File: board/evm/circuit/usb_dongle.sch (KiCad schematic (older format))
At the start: 1 part

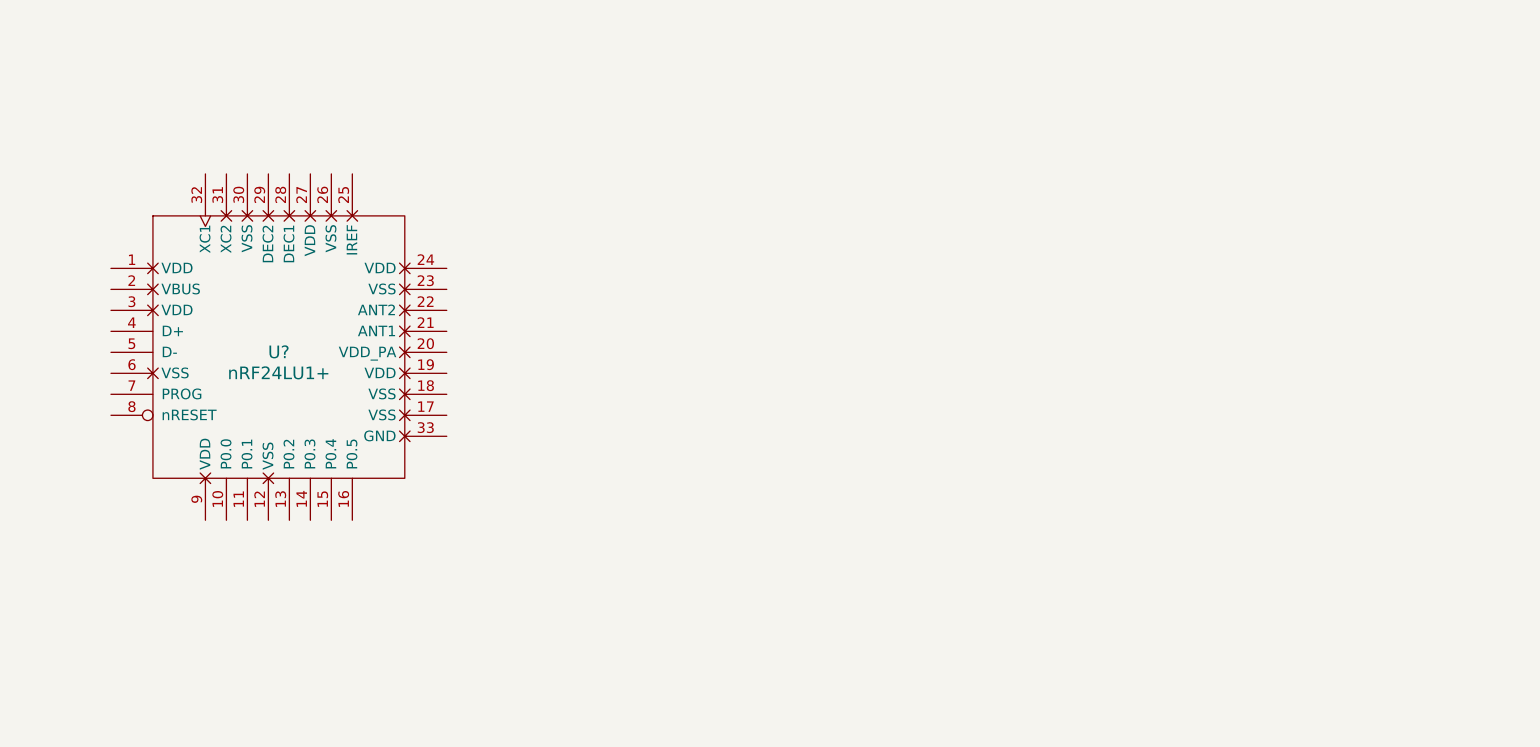
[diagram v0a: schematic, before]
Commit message: still working for sch
All done except for battery, which need more consideration on scheme of
QC2.0 (or QC3.0?), bidirectional charge.
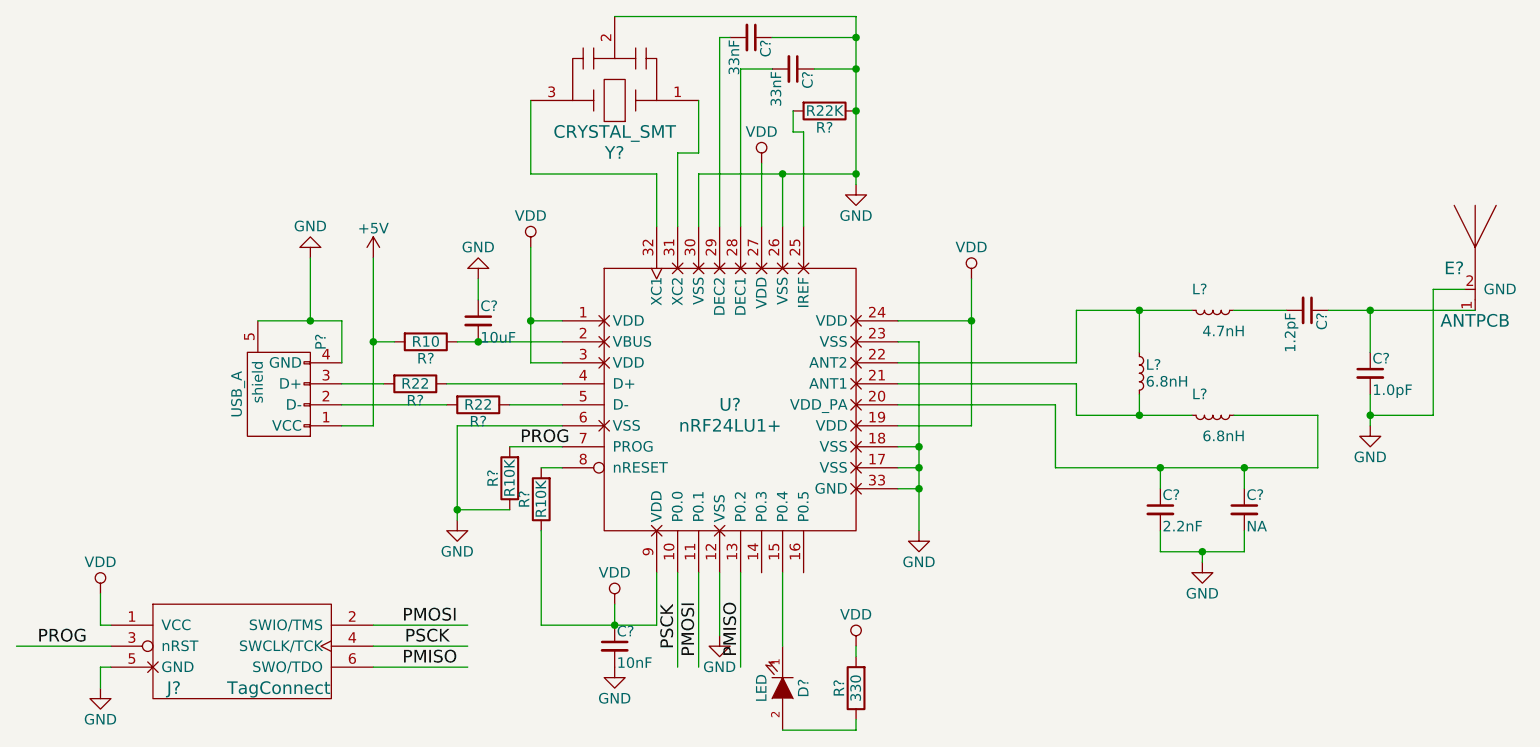
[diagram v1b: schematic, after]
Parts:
- added C?: 10uF, symbol C_Small
- added C?: 10nF, symbol C_Small
- added C? (x2): 33nF, symbol C_Small
- added C?: 2.2nF, symbol C_Small
- added C?: NA, symbol C_Small
- added C?: 1.2pF, symbol C_Small
- added C?: 1.0pF, symbol C_Small
- added D?: LED, symbol LED
- added E?: ANTPCB, symbol ANTPCB
- added J?: TagConnect, symbol TagConnect
- added L? (x2): 6.8nH, symbol L_Small
- added L?: 4.7nH, symbol L_Small
- added P?: USB_A, symbol USB_A
- added R? (x2): R22, symbol R
- added R?: R10, symbol R
- added R? (x2): R10K, symbol R
- added R?: R22K, symbol R
- added R?: 330, symbol R
- added Y?: CRYSTAL_SMT, symbol CRYSTAL_SMT
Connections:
- net labels added: +5V, GND, PMISO, PMOSI, PROG, PSCK, VDD
- wire segments 0 -> 117
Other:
- moved on the sheet: U?

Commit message: bug fix
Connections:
- wire segments 117 -> 95
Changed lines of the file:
@@
 LIBS:Altera
 LIBS:my_kicad
+LIBS:Oscillators
 LIBS:oh-my-keyboard-cache
 EELAYER 25 0
@@
 $Descr A3 16535 11693
 encoding utf-8
-Sheet 7 12
+Sheet 6 12
 Title ""
 Date ""
@@
 	4600 3100 4850 3100
 Wire Wire Line
-	3400 2700 3650 2700
-Wire Wire Line
-	3650 2700 3800 2700
+	3400 2700 3800 2700
 Wire Wire Line
 	3800 2700 3800 2900
@@
 	4850 2700 4700 2700
 Wire Wire Line
-	4700 2350 4700 2700
-Wire Wire Line
-	4700 2700 4700 2900
+	4700 2350 4700 2900
 Wire Wire Line
 	4700 2900 4850 2900
@@
 	4050 2800 3950 2800
 Wire Wire Line
-	4350 2800 4450 2800
-Wire Wire Line
-	4450 2800 4850 2800
+	4350 2800 4850 2800
 Connection ~ 4450 2800
 Wire Wire Line
-	3950 2400 3950 2800
-Wire Wire Line
-	3950 2800 3950 3200
+	3950 2400 3950 3200
 Wire Wire Line
 	4450 2600 4450 2500
@@
 	4850 3200 4350 3200
 Wire Wire Line
-	4350 3200 4350 3600
-Wire Wire Line
-	4350 3600 4350 3650
+	4350 3200 4350 3650
 Wire Wire Line
 	4600 3600 4350 3600
@@
 	4750 3700 4750 4150
 Wire Wire Line
-	4750 4150 5100 4150
-Wire Wire Line
-	5100 4150 5300 4150
+	4750 4150 5300 4150
 Wire Wire Line
 	5100 4150 5100 4050
@@
 	6450 3300 6550 3300
 Wire Wire Line
-	6550 2800 6550 3300
-Wire Wire Line
-	6550 3300 6550 3400
-Wire Wire Line
-	6550 3400 6550 3500
-Wire Wire Line
-	6550 3500 6550 3700
+	6550 2800 6550 3700
 Wire Wire Line
 	6450 3500 6550 3500
@@
 	6450 2700 6800 2700
 Wire Wire Line
-	6800 2500 6800 2700
-Wire Wire Line
-	6800 2700 6800 3200
+	6800 2500 6800 3200
 Wire Wire Line
 	6800 3200 6450 3200
@@
 	5500 2000 5500 2250
 Wire Wire Line
-	6250 2000 5900 2000
-Wire Wire Line
-	5900 2000 5500 2000
-Wire Wire Line
-	6250 1250 6250 1350
-Wire Wire Line
-	6250 1350 6250 1500
-Wire Wire Line
-	6250 1500 6250 1700
-Wire Wire Line
-	6250 1700 6250 2000
-Wire Wire Line
-	6250 2000 6250 2050
+	6250 2000 5500 2000
+Wire Wire Line
+	6250 1250 6250 2050
 Wire Wire Line
 	5900 2250 5900 2000
@@
 $EndComp
 Wire Wire Line
-	7300 2650 7600 2650
-Wire Wire Line
-	7600 2650 7850 2650
+	7300 2650 7850 2650
 Wire Wire Line
 	7600 2650 7600 2850
@@
 	7600 3050 7600 3150
 Wire Wire Line
-	7300 3150 7600 3150
-Wire Wire Line
-	7600 3150 7850 3150
+	7300 3150 7850 3150
 Wire Wire Line
 	6450 2900 7300 2900
@@
 	7200 3100 7200 3400
 Wire Wire Line
-	7200 3400 7700 3400
-Wire Wire Line
-	7700 3400 8100 3400
-Wire Wire Line
-	8100 3400 8450 3400
+	7200 3400 8450 3400
 Wire Wire Line
 	8450 3400 8450 3150
@@
 	7700 3700 7700 3800
 Wire Wire Line
-	7700 3800 7900 3800
-Wire Wire Line
-	7900 3800 8100 3800
+	7700 3800 8100 3800
 Wire Wire Line
 	8100 3800 8100 3700
@@
 $EndComp
 Wire Wire Line
-	8500 2650 8700 2650
-Wire Wire Line
-	8700 2650 9200 2650
+	8500 2650 9200 2650
 Wire Wire Line
 	8700 2650 8700 2850
@@
 $EndComp
 Wire Wire Line
-	8700 3050 8700 3150
-Wire Wire Line
-	8700 3150 8700 3200
+	8700 3050 8700 3200
 $Comp
 L ANTPCB E?

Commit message: working on drc
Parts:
- gave numbers to parts that had none: 24
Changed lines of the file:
@@
 $EndDescr
 $Comp
-L nRF24LU1+ U?
+L nRF24LU1+ U9
 U 1 1 5754763F
 P 5650 3100
-F 0 "U?" H 5650 3100 60  0000 C CNN
+F 0 "U9" H 5650 3100 60  0000 C CNN
 F 1 "nRF24LU1+" H 5650 3000 60  0000 C CNN
 F 2 "" H 5650 3100 60  0000 C CNN
@@
 $EndComp
 $Comp
-L USB_A P?
+L USB_A P2
 U 1 1 5758AC51
 P 3500 3000
-F 0 "P?" H 3700 2800 50  0000 C CNN
+F 0 "P2" H 3700 2800 50  0000 C CNN
 F 1 "USB_A" H 3450 3200 50  0000 C CNN
 F 2 "" V 3450 2900 50  0000 C CNN
@@
 $EndComp
 $Comp
-L R R?
+L R R8
 U 1 1 5758AF6E
 P 4150 3000
-F 0 "R?" V 4230 3000 50  0000 C CNN
+F 0 "R8" V 4230 3000 50  0000 C CNN
 F 1 "R22" V 4150 3000 50  0000 C CNN
 F 2 "" V 4080 3000 50  0000 C CNN
@@
 $EndComp
 $Comp
-L R R?
+L R R10
 U 1 1 5758AFBE
 P 4450 3100
-F 0 "R?" V 4530 3100 50  0000 C CNN
+F 0 "R10" V 4530 3100 50  0000 C CNN
 F 1 "R22" V 4450 3100 50  0000 C CNN
 F 2 "" V 4380 3100 50  0000 C CNN
@@
 $EndComp
 $Comp
-L GND #PWR?
+L GND #PWR080
 U 1 1 5758B050
 P 3650 2400
-F 0 "#PWR?" H 3650 2150 50  0001 C CNN
+F 0 "#PWR080" H 3650 2150 50  0001 C CNN
 F 1 "GND" H 3650 2250 50  0000 C CNN
 F 2 "" H 3650 2400 50  0000 C CNN
@@
 $EndComp
 $Comp
-L +5V #PWR?
+L +5V #PWR081
 U 1 1 5758B200
 P 3950 2400
-F 0 "#PWR?" H 3950 2250 50  0001 C CNN
+F 0 "#PWR081" H 3950 2250 50  0001 C CNN
 F 1 "+5V" H 3950 2540 50  0000 C CNN
 F 2 "" H 3950 2400 50  0000 C CNN
@@
 $EndComp
 $Comp
-L C_Small C?
+L C_Small C28
 U 1 1 5758B23D
 P 4450 2700
-F 0 "C?" H 4460 2770 50  0000 L CNN
+F 0 "C28" H 4460 2770 50  0000 L CNN
 F 1 "10uF" H 4460 2620 50  0000 L CNN
 F 2 "" H 4450 2700 50  0000 C CNN
@@
 $EndComp
 $Comp
-L R R?
+L R R9
 U 1 1 5758B396
 P 4200 2800
-F 0 "R?" V 4280 2800 50  0000 C CNN
+F 0 "R9" V 4280 2800 50  0000 C CNN
 F 1 "R10" V 4200 2800 50  0000 C CNN
 F 2 "" V 4130 2800 50  0000 C CNN
@@
 $EndComp
 $Comp
-L GND #PWR?
+L GND #PWR082
 U 1 1 5758B547
 P 4450 2500
-F 0 "#PWR?" H 4450 2250 50  0001 C CNN
+F 0 "#PWR082" H 4450 2250 50  0001 C CNN
 F 1 "GND" H 4450 2350 50  0000 C CNN
 F 2 "" H 4450 2500 50  0000 C CNN
@@
 $EndComp
 $Comp
-L GND #PWR?
+L GND #PWR083
 U 1 1 5758B5D1
 P 4350 3650
-F 0 "#PWR?" H 4350 3400 50  0001 C CNN
+F 0 "#PWR083" H 4350 3400 50  0001 C CNN
 F 1 "GND" H 4350 3500 50  0000 C CNN
 F 2 "" H 4350 3650 50  0000 C CNN
@@
 $EndComp
 $Comp
-L R R?
+L R R11
 U 1 1 5758B6D5
 P 4600 3450
-F 0 "R?" V 4680 3450 50  0000 C CNN
+F 0 "R11" V 4680 3450 50  0000 C CNN
 F 1 "R10K" V 4600 3450 50  0000 C CNN
 F 2 "" V 4530 3450 50  0000 C CNN
@@
 $EndComp
 $Comp
-L R R?
+L R R12
 U 1 1 5758B784
 P 4750 3550
-F 0 "R?" V 4830 3550 50  0000 C CNN
+F 0 "R12" V 4830 3550 50  0000 C CNN
 F 1 "R10K" V 4750 3550 50  0000 C CNN
 F 2 "" V 4680 3550 50  0000 C CNN
@@
 $EndComp
 $Comp
-L C_Small C?
+L C_Small C29
 U 1 1 5758BA18
 P 5100 4250
-F 0 "C?" H 5110 4320 50  0000 L CNN
+F 0 "C29" H 5110 4320 50  0000 L CNN
 F 1 "10nF" H 5110 4170 50  0000 L CNN
 F 2 "" H 5100 4250 50  0000 C CNN
@@
 $EndComp
 $Comp
-L GND #PWR?
+L GND #PWR084
 U 1 1 5758BAA4
 P 5100 4350
-F 0 "#PWR?" H 5100 4100 50  0001 C CNN
+F 0 "#PWR084" H 5100 4100 50  0001 C CNN
 F 1 "GND" H 5100 4200 50  0000 C CNN
 F 2 "" H 5100 4350 50  0000 C CNN
@@
 $EndComp
 $Comp
-L GND #PWR?
+L GND #PWR085
 U 1 1 5758BAF2
 P 5600 4200
-F 0 "#PWR?" H 5600 3950 50  0001 C CNN
+F 0 "#PWR085" H 5600 3950 50  0001 C CNN
 F 1 "GND" H 5600 4050 50  0000 C CNN
 F 2 "" H 5600 4200 50  0000 C CNN
@@
 $EndComp
 $Comp
-L GND #PWR?
+L GND #PWR086
 U 1 1 5758BCC4
 P 6550 3700
-F 0 "#PWR?" H 6550 3450 50  0001 C CNN
+F 0 "#PWR086" H 6550 3450 50  0001 C CNN
 F 1 "GND" H 6550 3550 50  0000 C CNN
 F 2 "" H 6550 3700 50  0000 C CNN
@@
 $EndComp
 $Comp
-L GND #PWR?
+L GND #PWR087
 U 1 1 5758BFC5
 P 6250 2050
-F 0 "#PWR?" H 6250 1800 50  0001 C CNN
+F 0 "#PWR087" H 6250 1800 50  0001 C CNN
 F 1 "GND" H 6250 1900 50  0000 C CNN
 F 2 "" H 6250 2050 50  0000 C CNN
@@
 Connection ~ 5900 2000
 $Comp
-L CRYSTAL_SMT Y?
+L CRYSTAL_SMT Y3
 U 1 1 5758C1C1
 P 5100 1600
-F 0 "Y?" H 5100 1900 60  0000 C CNN
+F 0 "Y3" H 5100 1900 60  0000 C CNN
 F 1 "CRYSTAL_SMT" H 5100 1800 60  0000 C CNN
 F 2 "" H 5100 1600 60  0000 C CNN
@@
 Connection ~ 6250 2000
 $Comp
-L C_Small C?
+L C_Small C30
 U 1 1 5758C579
 P 5750 1350
-F 0 "C?" H 5760 1420 50  0000 L CNN
+F 0 "C30" H 5760 1420 50  0000 L CNN
 F 1 "33nF" H 5760 1270 50  0000 L CNN
 F 2 "" H 5750 1350 50  0000 C CNN
@@
 	5600 1350 5650 1350
 $Comp
-L C_Small C?
+L C_Small C31
 U 1 1 5758C690
 P 5950 1500
-F 0 "C?" H 5960 1570 50  0000 L CNN
+F 0 "C31" H 5960 1570 50  0000 L CNN
 F 1 "33nF" H 5960 1420 50  0000 L CNN
 F 2 "" H 5950 1500 50  0000 C CNN
@@
 Connection ~ 6250 1500
 $Comp
-L R R?
+L R R13
 U 1 1 5758C7CB
 P 6100 1700
-F 0 "R?" V 6180 1700 50  0000 C CNN
+F 0 "R13" V 6180 1700 50  0000 C CNN
 F 1 "R22K" V 6100 1700 50  0000 C CNN
 F 2 "" V 6030 1700 50  0000 C CNN
@@
 Connection ~ 6250 1700
 $Comp
-L L_Small L?
+L L_Small L7
 U 1 1 5758CBB0
 P 7600 2950
-F 0 "L?" H 7630 2990 50  0000 L CNN
+F 0 "L7" H 7630 2990 50  0000 L CNN
 F 1 "6.8nH" H 7630 2910 50  0000 L CNN
 F 2 "" H 7600 2950 50  0000 C CNN
@@
 $EndComp
 $Comp
-L L_Small L?
+L L_Small L8
 U 1 1 5758CC1D
 P 7950 2650
-F 0 "L?" V 7850 2550 50  0000 L CNN
+F 0 "L8" V 7850 2550 50  0000 L CNN
 F 1 "4.7nH" V 8050 2600 50  0000 L CNN
 F 2 "" H 7950 2650 50  0000 C CNN
@@
 $EndComp
 $Comp
-L L_Small L?
+L L_Small L9
 U 1 1 5758CD4B
 P 7950 3150
-F 0 "L?" V 7850 3050 50  0000 L CNN
+F 0 "L9" V 7850 3050 50  0000 L CNN
 F 1 "6.8nH" V 8050 3100 50  0000 L CNN
 F 2 "" H 7950 3150 50  0000 C CNN
@@
 	8450 3150 8050 3150
 $Comp
-L C_Small C?
+L C_Small C32
 U 1 1 5758CFF2
 P 7700 3600
-F 0 "C?" H 7710 3670 50  0000 L CNN
+F 0 "C32" H 7710 3670 50  0000 L CNN
 F 1 "2.2nF" H 7710 3520 50  0000 L CNN
 F 2 "" H 7700 3600 50  0000 C CNN
@@
 $EndComp
 $Comp
-L C_Small C?
+L C_Small C33
 U 1 1 5758D097
 P 8100 3600
-F 0 "C?" H 8110 3670 50  0000 L CNN
+F 0 "C33" H 8110 3670 50  0000 L CNN
 F 1 "NA" H 8110 3520 50  0000 L CNN
 F 2 "" H 8100 3600 50  0000 C CNN
@@
 	8100 3800 8100 3700
 $Comp
-L GND #PWR?
+L GND #PWR088
 U 1 1 5758D27C
 P 7900 3850
-F 0 "#PWR?" H 7900 3600 50  0001 C CNN
+F 0 "#PWR088" H 7900 3600 50  0001 C CNN
 F 1 "GND" H 7900 3700 50  0000 C CNN
 F 2 "" H 7900 3850 50  0000 C CNN
@@
 Connection ~ 7900 3800
 $Comp
-L C_Small C?
+L C_Small C34
 U 1 1 5758D32D
 P 8400 2650
-F 0 "C?" H 8410 2720 50  0000 L CNN
+F 0 "C34" H 8410 2720 50  0000 L CNN
 F 1 "1.2pF" H 8410 2570 50  0000 L CNN
 F 2 "" H 8400 2650 50  0000 C CNN
@@
 	8300 2650 8050 2650
 $Comp
-L C_Small C?
+L C_Small C35
 U 1 1 5758D43B
 P 8700 2950
-F 0 "C?" H 8710 3020 50  0000 L CNN
+F 0 "C35" H 8710 3020 50  0000 L CNN
 F 1 "1.0pF" H 8710 2870 50  0000 L CNN
 F 2 "" H 8700 2950 50  0000 C CNN
@@
 	8700 2650 8700 2850
 $Comp
-L GND #PWR?
+L GND #PWR089
 U 1 1 5758D552
 P 8700 3200
-F 0 "#PWR?" H 8700 2950 50  0001 C CNN
+F 0 "#PWR089" H 8700 2950 50  0001 C CNN
 F 1 "GND" H 8700 3050 50  0000 C CNN
 F 2 "" H 8700 3200 50  0000 C CNN
@@
 	8700 3050 8700 3200
 $Comp
-L ANTPCB E?
+L ANTPCB E3
 U 1 1 5758D612
 P 9200 2600
-F 0 "E?" H 9100 2750 60  0000 C CNN
+F 0 "E3" H 9100 2750 60  0000 C CNN
 F 1 "ANTPCB" H 9200 2500 60  0000 C CNN
 F 2 "" H 9200 2600 60  0000 C CNN
@@
 Connection ~ 8700 3150
 $Comp
-L VDD #PWR?
+L VDD #PWR090
 U 1 1 5758DAF7
 P 4700 2350
-F 0 "#PWR?" H 4700 2200 50  0001 C CNN
+F 0 "#PWR090" H 4700 2200 50  0001 C CNN
 F 1 "VDD" H 4700 2500 50  0000 C CNN
 F 2 "" H 4700 2350 50  0000 C CNN
@@
 $EndComp
 $Comp
-L VDD #PWR?
+L VDD #PWR091
 U 1 1 5758DB5E
 P 5100 4050
-F 0 "#PWR?" H 5100 3900 50  0001 C CNN
+F 0 "#PWR091" H 5100 3900 50  0001 C CNN
 F 1 "VDD" H 5100 4200 50  0000 C CNN
 F 2 "" H 5100 4050 50  0000 C CNN
@@
 $EndComp
 $Comp
-L VDD #PWR?
+L VDD #PWR092
 U 1 1 5758DBBE
 P 6800 2500
-F 0 "#PWR?" H 6800 2350 50  0001 C CNN
+F 0 "#PWR092" H 6800 2350 50  0001 C CNN
 F 1 "VDD" H 6800 2650 50  0000 C CNN
 F 2 "" H 6800 2500 50  0000 C CNN
@@
 $EndComp
 $Comp
-L VDD #PWR?
+L VDD #PWR093
 U 1 1 5758DC1E
 P 5800 1950
-F 0 "#PWR?" H 5800 1800 50  0001 C CNN
+F 0 "#PWR093" H 5800 1800 50  0001 C CNN
 F 1 "VDD" H 5800 2100 50  0000 C CNN
 F 2 "" H 5800 1950 50  0000 C CNN
@@
 $EndComp
 $Comp
-L VDD #PWR?
+L VDD #PWR094
 U 1 1 5758DC68
 P 6250 4250
-F 0 "#PWR?" H 6250 4100 50  0001 C CNN
+F 0 "#PWR094" H 6250 4100 50  0001 C CNN
 F 1 "VDD" H 6250 4400 50  0000 C CNN
 F 2 "" H 6250 4250 50  0000 C CNN
@@
 $EndComp
 $Comp
-L R R?
+L R R14
 U 1 1 5758DCB2
 P 6250 4450
-F 0 "R?" V 6330 4450 50  0000 C CNN
+F 0 "R14" V 6330 4450 50  0000 C CNN
 F 1 "330" V 6250 4450 50  0000 C CNN
 F 2 "" V 6180 4450 50  0000 C CNN
@@
 $EndComp
 $Comp
-L LED D?
+L LED D10
 U 1 1 5758DD84
 P 5900 4450
-F 0 "D?" H 5900 4550 50  0000 C CNN
+F 0 "D10" H 5900 4550 50  0000 C CNN
 F 1 "LED" H 5900 4350 50  0000 C CNN
 F 2 "" H 5900 4450 50  0000 C CNN
@@
 	6250 4300 6250 4250
 $Comp
-L TagConnect J?
+L TagConnect J3
 U 1 1 5758DFC7
 P 3300 4300
-F 0 "J?" H 3000 4150 60  0000 C CNN
+F 0 "J3" H 3000 4150 60  0000 C CNN
 F 1 "TagConnect" H 3500 4150 60  0000 C CNN
 F 2 "" H 3150 4350 60  0000 C CNN
@@
 $EndComp
 $Comp
-L VDD #PWR?
+L VDD #PWR095
 U 1 1 5758E07A
 P 2650 4000
-F 0 "#PWR?" H 2650 3850 50  0001 C CNN
+F 0 "#PWR095" H 2650 3850 50  0001 C CNN
 F 1 "VDD" H 2650 4150 50  0000 C CNN
 F 2 "" H 2650 4000 50  0000 C CNN
@@
 	2650 4150 2700 4150
 $Comp
-L GND #PWR?
+L GND #PWR096
 U 1 1 5758E152
 P 2650 4450
-F 0 "#PWR?" H 2650 4200 50  0001 C CNN
+F 0 "#PWR096" H 2650 4200 50  0001 C CNN
 F 1 "GND" H 2650 4300 50  0000 C CNN
 F 2 "" H 2650 4450 50  0000 C CNN
